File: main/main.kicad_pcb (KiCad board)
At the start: 2 copper layers, 31.2 x 55.4 mm, 23 parts, among them IC1 MB1010-000, M1 Motor_DC, P1 Digital, P2 Analog, P3 CONN_01X01, P4 CONN_01X01, P5 CONN_01X01, P6 CONN_01X01, Q1 PN2222A, U1 SW_PWR_BTN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

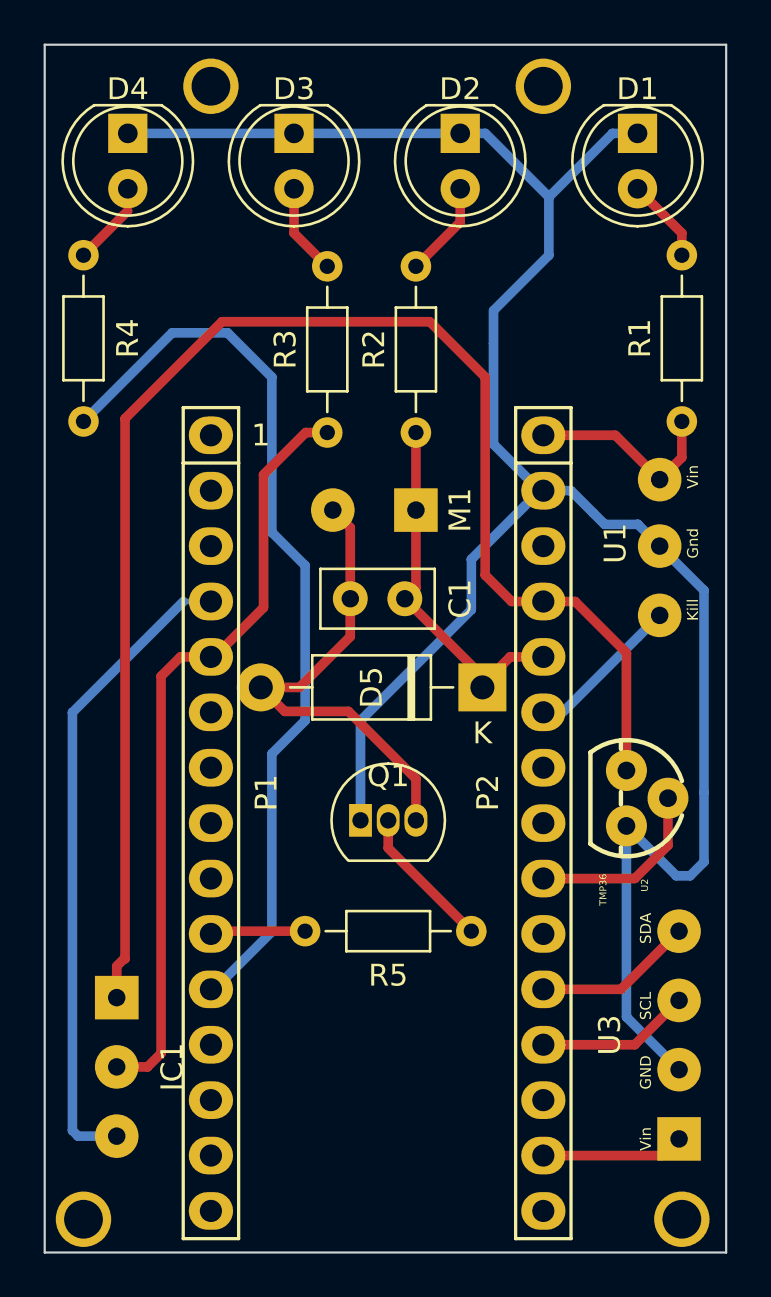
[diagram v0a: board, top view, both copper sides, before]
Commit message: main.pcb: Reassigned pins because A7 is input ONLY
New pin assignment:

A6 - Temperature input
A4 - Motor Output Control
A5 - Kill Power
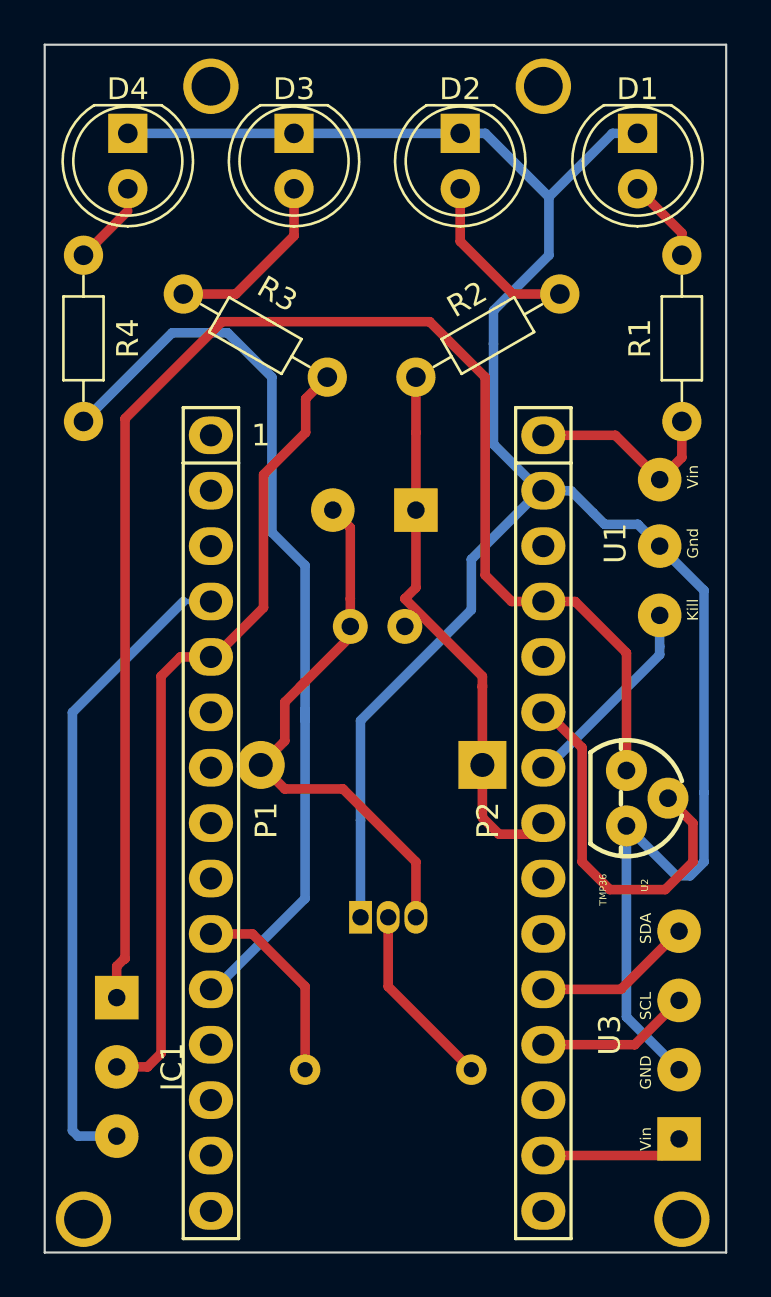
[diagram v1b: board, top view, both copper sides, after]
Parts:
- C1, D5, M1, Q1, R5: moved to B.Cu
- moved R5 6.35 mm to (149.9, 102.2)
- moved Q1 4.44 mm to (152.4, 95.2)
- moved D5 3.56 mm to (158.0, 88.3)
- moved R2 2.54 mm to (154.9, 70.5), turned to 30 degrees
- moved R3 2.54 mm to (150.9, 70.5), turned to 150 degrees
- moved C1 1.27 mm to (154.4, 81.9)
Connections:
- C1 pad 1: /A7 -> /A4
- D5 pad 1: /A7 -> /A4
- M1 pad 1: /A7 -> /A4
- R2 pad 1: /A7 -> /A4
- U1 pad 4: /A6 -> /A5
- U2 pad 2: /A3 -> /A6
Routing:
- net /A4: track 0.00 -> 25.3 mm
- net /A7: track 16.8 -> 0.00 mm
- net /A6: track 8.06 -> 19.0 mm
- net /A5: track 0.00 -> 9.28 mm
- net /A3: track 8.51 -> 0.00 mm
- net /7: track 4.37 -> 9.31 mm
- net GND: track 129.5 -> 134.0 mm
- net Net-(D3-Pad2): track 4.19 -> 8.34 mm
- net Net-(C1-Pad2): track 22.0 -> 25.6 mm
- net Net-(D2-Pad2): track 4.40 -> 7.98 mm
- net /2: track 35.5 -> 37.5 mm
- net Net-(Q1-Pad2): track 6.66 -> 8.56 mm
- net /8: track 41.7 -> 42.2 mm
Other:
- net class Default: trace_width 0.25 -> 0.44

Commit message: main.pcb: Reassigned pins to reserve A4 and A5 for accelerometer
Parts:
- moved U2 3.43 mm to (164.5, 86.4)
- moved U3 2.84 mm to (165.7, 102.9)
- moved Q1 2.54 mm to (152.4, 97.8)
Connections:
- C1 pad 1: /A4 -> /A2
- D5 pad 1: /A4 -> /A2
- M1 pad 1: /A4 -> /A2
- R2 pad 1: /A4 -> /A2
- U1 pad 4: /A5 -> /A3
- U3 pad 4: /A1 -> /A5
- U3 pad 6: /A0 -> /A4
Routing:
- net /A2: track 0.00 -> 28.6 mm
- net /A4: track 25.3 -> 8.75 mm
- net /A3: track 0.00 -> 14.4 mm
- net /A1: track 7.33 -> 0.00 mm
- net /A0: track 7.22 -> 0.15 mm
- net /A6: track 19.0 -> 14.0 mm
- net +5V: track 68.6 -> 65.3 mm
- net Net-(C1-Pad2): track 25.6 -> 28.1 mm
- net Net-(Q1-Pad2): track 8.56 -> 6.35 mm
- net /A5: track 9.28 -> 7.31 mm
- net GND: track 134.0 -> 134.7 mm
- net +3V3: track 6.54 -> 7.16 mm

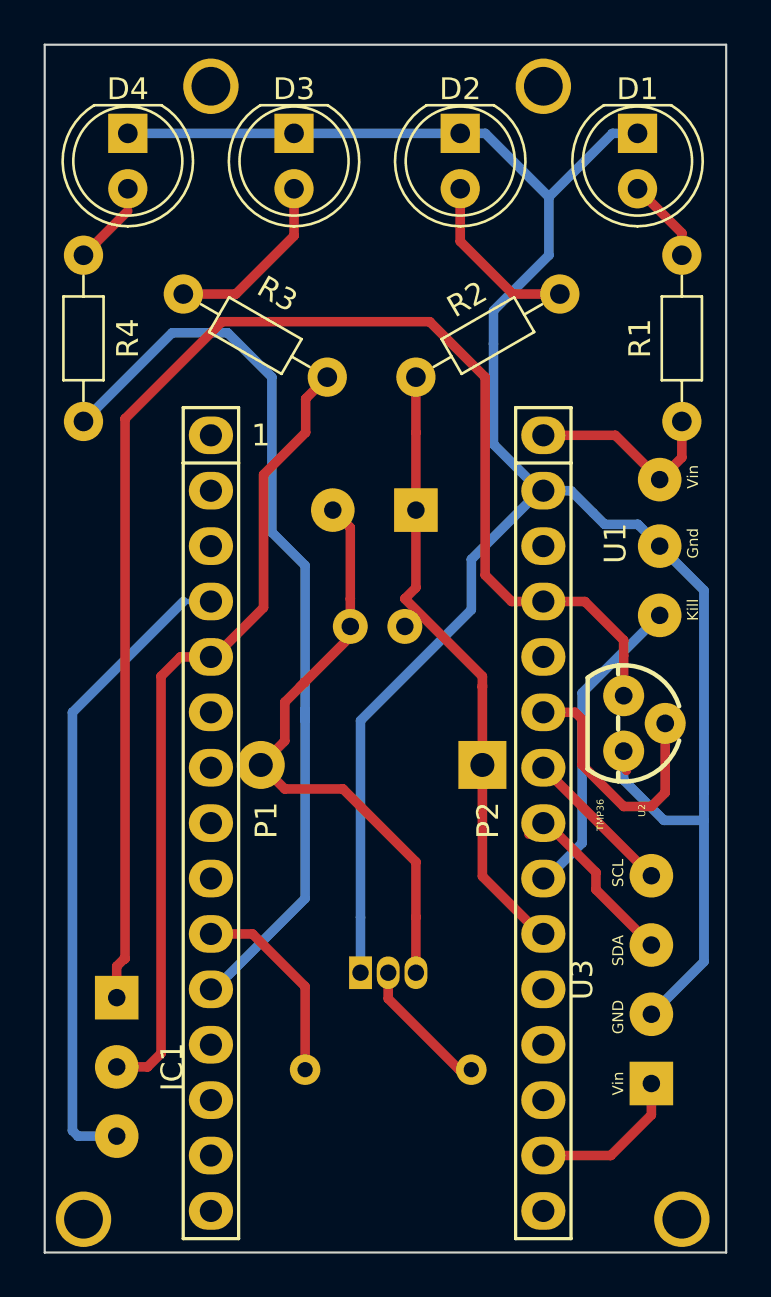
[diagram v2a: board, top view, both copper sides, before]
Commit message: main.pcb: Resolved disconnections and stray traces using Design Rules Check
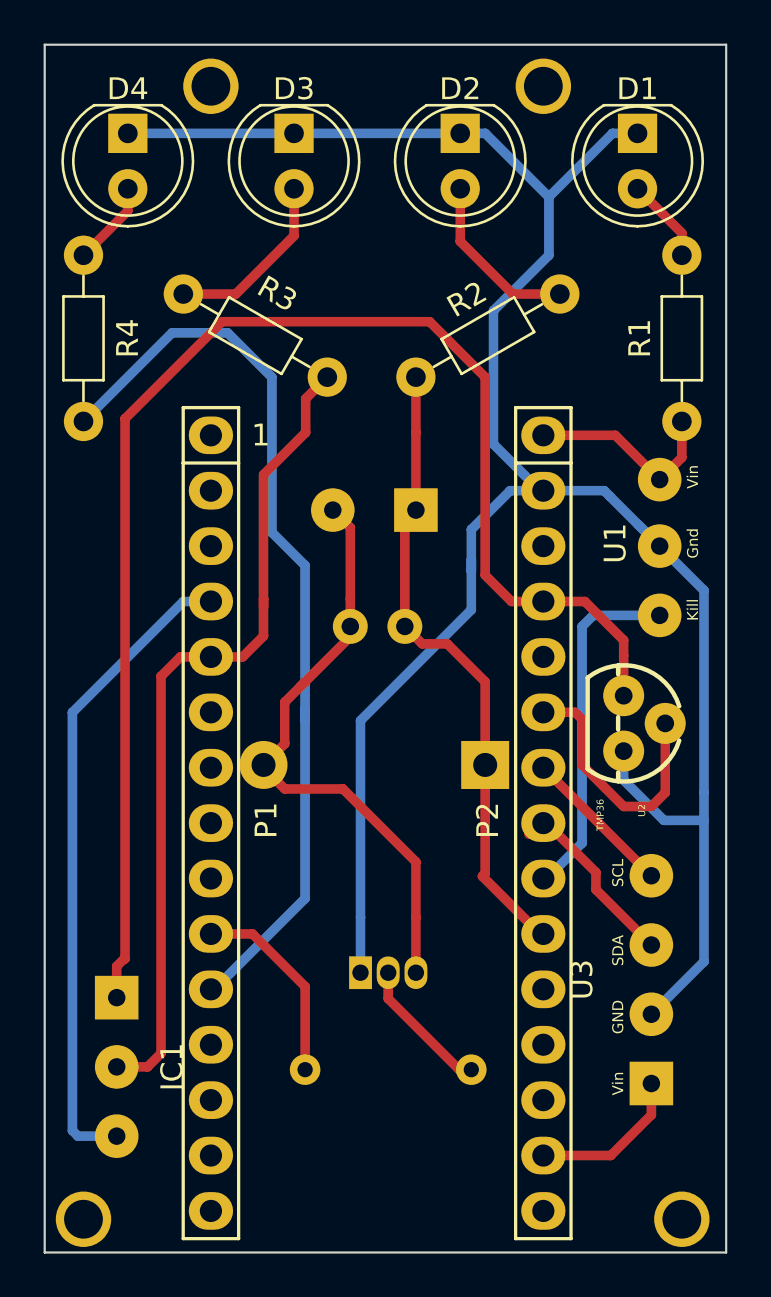
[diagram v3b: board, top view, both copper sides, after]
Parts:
- moved D5 0.13 mm to (158.1, 88.3)
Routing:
- net /A6: track 14.0 -> 12.0 mm
- net /A3: track 14.4 -> 16.1 mm
- net /2: track 37.5 -> 38.5 mm
- net /A2: track 28.6 -> 29.2 mm

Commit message: main.sch: Replaced 5V line with D3 to control turn ON/OFF ultrasonic sensor
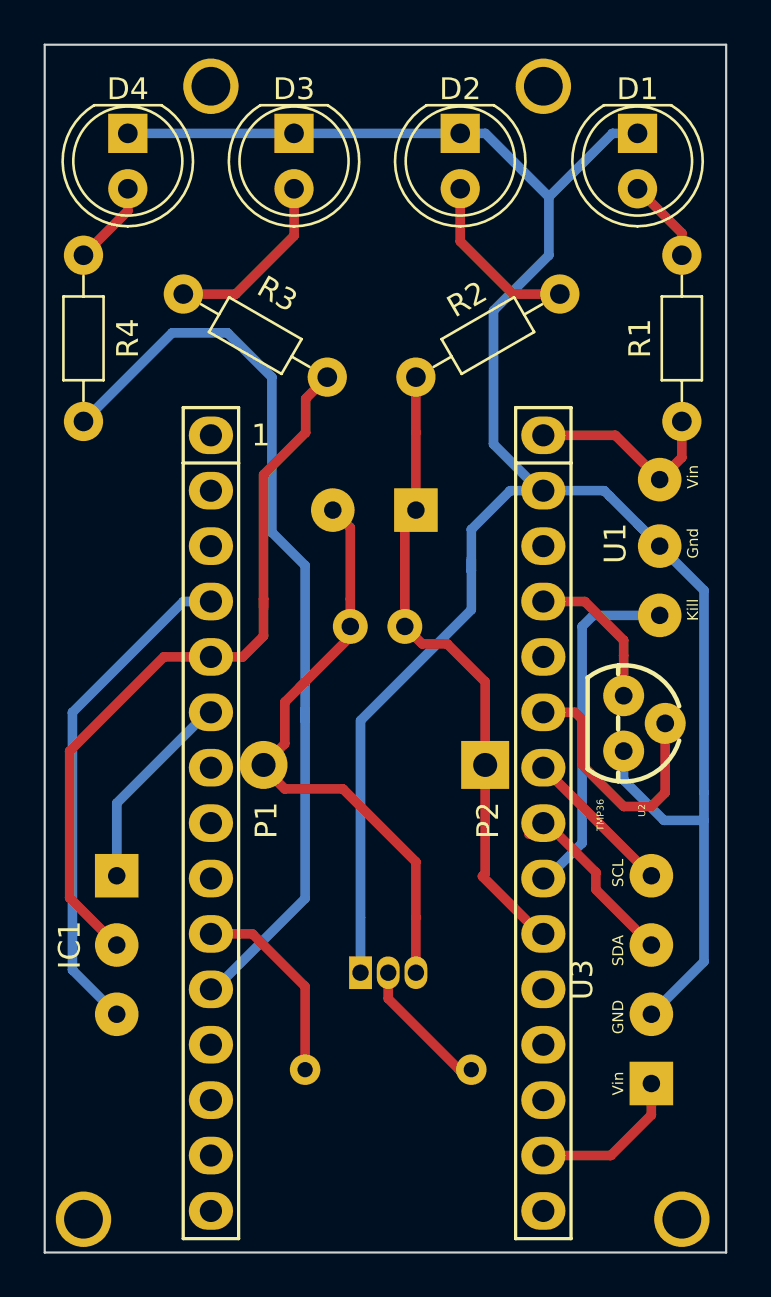
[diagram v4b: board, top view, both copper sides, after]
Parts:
- moved IC1 5.59 mm to (141.2, 93.3)
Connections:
- IC1 pad 6: +5V -> /3(**)
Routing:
- net +5V: track 65.3 -> 6.96 mm
- net /3(**): track 0.00 -> 9.37 mm
- net GND: track 134.8 -> 128.2 mm
- net /2: track 38.5 -> 34.3 mm
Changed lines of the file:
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@@
     (thickness 1.6)
     (drawings 20)
-    (tracks 143)
+    (tracks 134)
     (zones 0)
     (modules 23)
@@
   )
   (module MB1010:SolderWirePad_1x03_P3.175mm_Drill0.8mm (layer F.Cu)
-    (at 141.224 98.933 270)
+    (at 141.224 93.345 270)
     (descr "Wire solder connection")
     (tags connector)
     (attr virtual)
-    (fp_text reference IC1 (at 3.175 -2.54 270) (layer F.SilkS)
+    (fp_text reference IC1 (at 3.175 2.159 270) (layer F.SilkS)
       (effects (font (size 1 1) (thickness 0.15)))
     )
@@
     (fp_line (start 7.85 1.5) (end -1.49 1.5) (layer F.CrtYd) (width 0.05))
     (pad 6 thru_hole rect (at 0 0 270) (size 1.99898 1.99898) (drill 0.8001) (layers *.Cu *.Mask)
-      (net 15 +5V))
+      (net 6 "/3(**)"))
     (pad 2 thru_hole circle (at 3.175 0 270) (size 1.99898 1.99898) (drill 0.8001) (layers *.Cu *.Mask)
       (net 5 /2))
@@
     (descr "Resistor, Axial_DIN0204 series, Axial, Horizontal, pin pitch=7.62mm, 0.167W, length*diameter=3.6*1.6mm^2, http://cdn-reichelt.de/documents/datenblatt/B400/1_4W%23YAG.pdf")
     (tags "Resistor Axial_DIN0204 series Axial Horizontal pin pitch 7.62mm 0.167W length 3.6mm diameter 1.6mm")
-    (fp_text reference R5 (at 3.81 -2.032) (layer B.SilkS)
+    (fp_text reference R5 (at 3.81 1.905) (layer B.SilkS)
       (effects (font (size 1 1) (thickness 0.15)) (justify mirror))
     )
@@
   (segment (start 149.352 59.309) (end 141.732 59.309) (width 0.44) (layer B.Cu) (net 4))
   (segment (start 144.276 80.772) (end 139.192 85.856) (width 0.44) (layer B.Cu) (net 4))
-  (segment (start 139.192 85.856) (end 139.192 105.029) (width 0.44) (layer B.Cu) (net 4))
-  (segment (start 139.446 105.283) (end 141.224 105.283) (width 0.44) (layer B.Cu) (net 4))
-  (segment (start 139.192 105.029) (end 139.446 105.283) (width 0.44) (layer B.Cu) (net 4))
   (segment (start 166.116 78.232) (end 165.116511 77.232511) (width 0.44) (layer B.Cu) (net 4))
   (segment (start 168.148 80.264) (end 168.148 89.535) (width 0.44) (layer B.Cu) (net 4))
@@
   (segment (start 157.48 79.375) (end 157.48 81.153) (width 0.44) (layer B.Cu) (net 4))
   (segment (start 158.496 73.5584) (end 160.6296 75.692) (width 0.44) (layer B.Cu) (net 4))
-  (segment (start 142.637492 102.108) (end 143.256 101.489492) (width 0.44) (layer F.Cu) (net 5))
-  (segment (start 141.224 102.108) (end 142.637492 102.108) (width 0.44) (layer F.Cu) (net 5))
-  (segment (start 143.256 101.489492) (end 143.256 84.201) (width 0.44) (layer F.Cu) (net 5))
-  (segment (start 144.145 83.312) (end 145.542 83.312) (width 0.44) (layer F.Cu) (net 5))
-  (segment (start 143.256 84.201) (end 144.145 83.312) (width 0.44) (layer F.Cu) (net 5))
+  (segment (start 139.192 97.663) (end 141.224 99.695) (width 0.44) (layer B.Cu) (net 4))
+  (segment (start 139.192 85.856) (end 139.192 97.663) (width 0.44) (layer B.Cu) (net 4))
   (segment (start 149.886051 73.025) (end 147.955 74.956051) (width 0.44) (layer F.Cu) (net 5))
   (segment (start 149.886051 71.474949) (end 150.876 70.485) (width 0.44) (layer F.Cu) (net 5))
@@
   (segment (start 147.955 74.956051) (end 147.955 80.645) (width 0.44) (layer F.Cu) (net 5))
   (segment (start 147.955 80.645) (end 147.955 81.0514) (width 0.44) (layer F.Cu) (net 5))
+  (segment (start 139.065 94.361) (end 141.224 96.52) (width 0.44) (layer F.Cu) (net 5))
+  (segment (start 139.065 87.63) (end 139.065 94.361) (width 0.44) (layer F.Cu) (net 5))
+  (segment (start 145.542 83.312) (end 143.383 83.312) (width 0.44) (layer F.Cu) (net 5))
+  (segment (start 143.383 83.312) (end 139.065 87.63) (width 0.44) (layer F.Cu) (net 5))
+  (segment (start 145.3896 85.852) (end 145.542 85.852) (width 0.44) (layer B.Cu) (net 6))
+  (segment (start 141.224 90.0176) (end 145.3896 85.852) (width 0.44) (layer B.Cu) (net 6))
+  (segment (start 141.224 90.0176) (end 141.224 93.345) (width 0.44) (layer B.Cu) (net 6))
   (segment (start 145.669 95.885) (end 145.542 96.012) (width 0.44) (layer F.Cu) (net 10))
   (segment (start 147.447 96.012) (end 145.542 96.012) (width 0.44) (layer F.Cu) (net 10))
@@
   (segment (start 167.132 74.168) (end 166.116 75.184) (width 0.44) (layer F.Cu) (net 14))
   (segment (start 167.132 72.517) (end 167.132 74.168) (width 0.44) (layer F.Cu) (net 14))
-  (segment (start 159.326 80.772) (end 158.115 79.561) (width 0.44) (layer F.Cu) (net 15))
-  (segment (start 160.782 80.772) (end 159.326 80.772) (width 0.44) (layer F.Cu) (net 15))
-  (segment (start 158.115 79.561) (end 158.115 70.485) (width 0.44) (layer F.Cu) (net 15))
-  (segment (start 158.115 70.485) (end 155.575 67.945) (width 0.44) (layer F.Cu) (net 15))
-  (segment (start 155.575 67.945) (end 146.05 67.945) (width 0.44) (layer F.Cu) (net 15))
-  (segment (start 146.05 67.945) (end 141.605 72.39) (width 0.44) (layer F.Cu) (net 15))
-  (segment (start 141.605 72.39) (end 141.605 97.155) (width 0.44) (layer F.Cu) (net 15))
-  (segment (start 141.224 97.49351) (end 141.224 98.933) (width 0.44) (layer F.Cu) (net 15))
-  (segment (start 141.56251 97.155) (end 141.224 97.49351) (width 0.44) (layer F.Cu) (net 15))
-  (segment (start 141.605 97.155) (end 141.56251 97.155) (width 0.44) (layer F.Cu) (net 15))
   (segment (start 164.465 83.253) (end 164.465 85.09) (width 0.44) (layer F.Cu) (net 15))
   (segment (start 160.782 80.772) (end 162.687 80.772) (width 0.44) (layer F.Cu) (net 15))
